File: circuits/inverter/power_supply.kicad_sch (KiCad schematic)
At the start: 44 parts

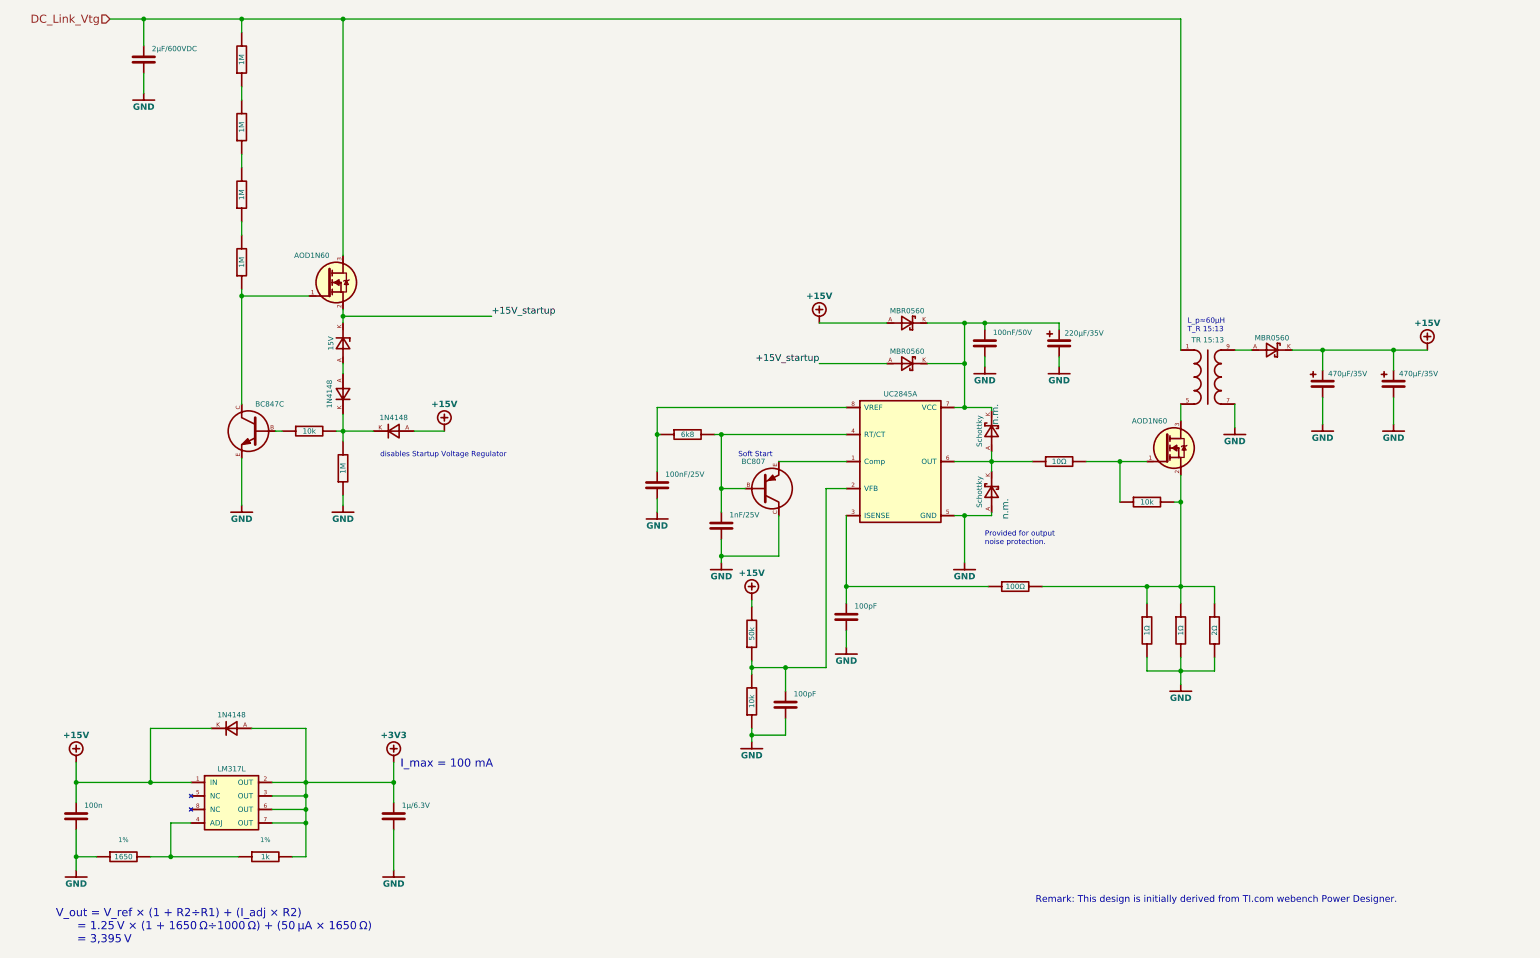
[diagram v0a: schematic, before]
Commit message: converts libraries to Kicad 6 format, updates bridge driver
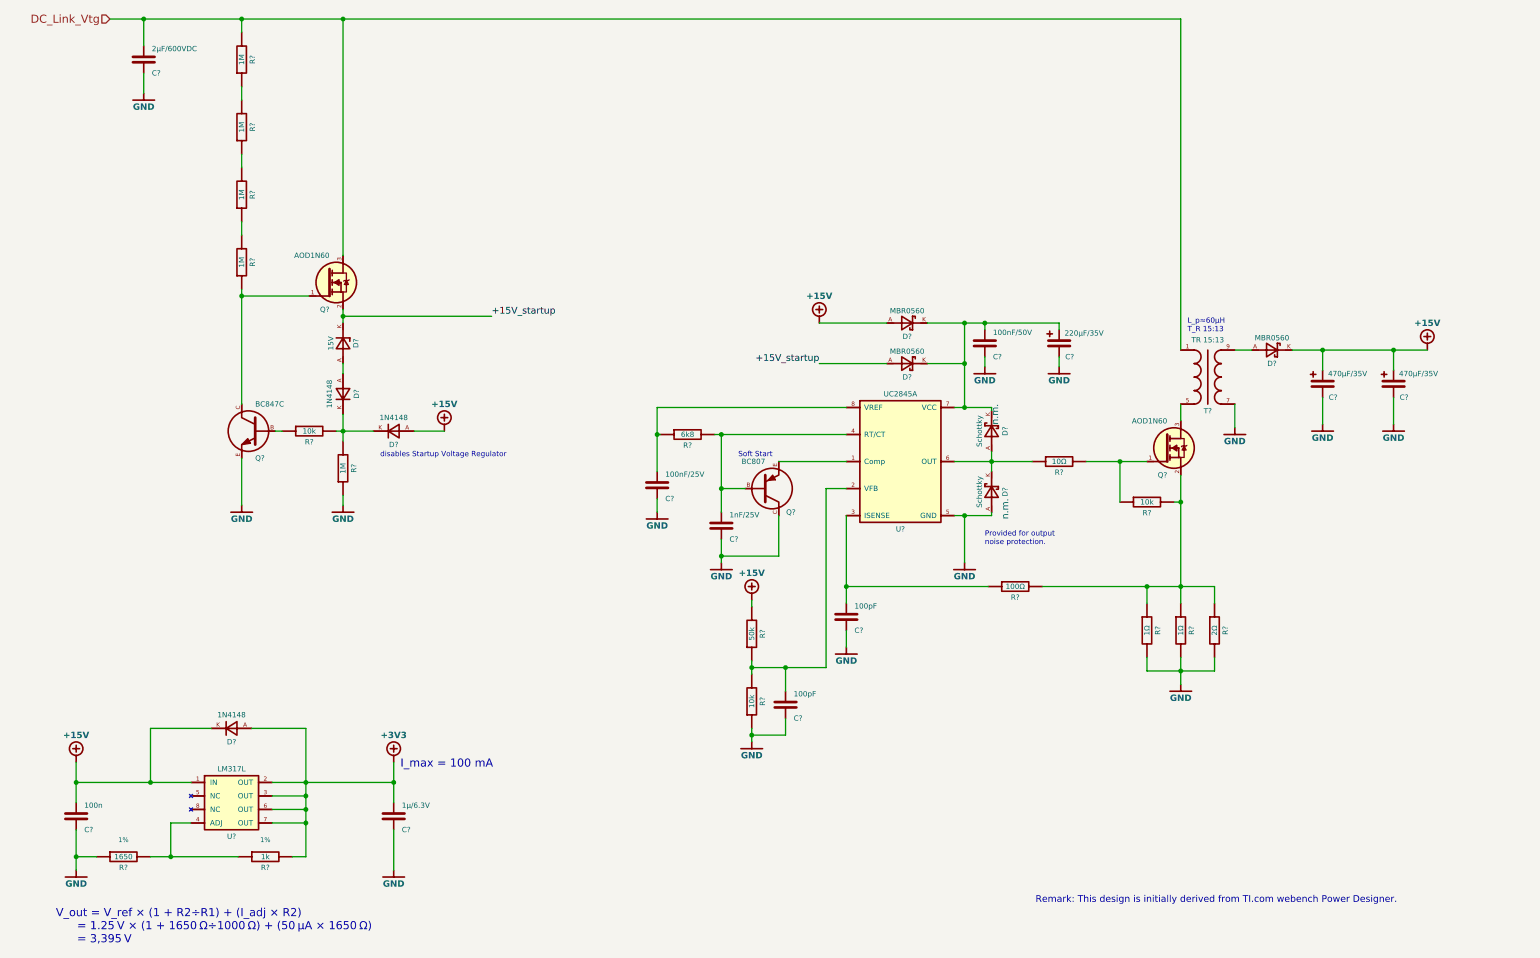
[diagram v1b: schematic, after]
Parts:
- gave numbers to parts that had none: 6

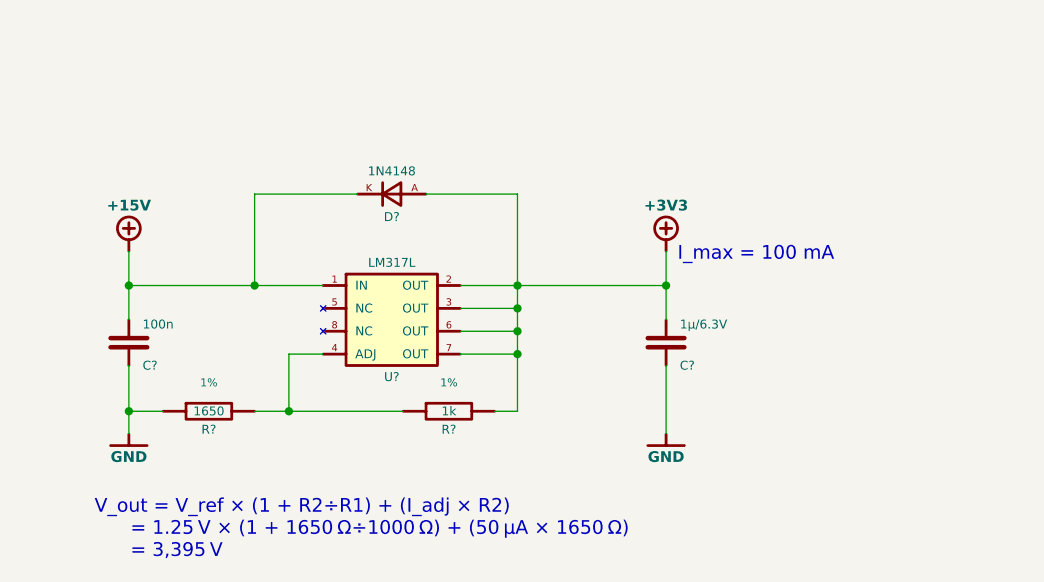
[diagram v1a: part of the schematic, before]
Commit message: updates circuits, adds linear regulator NCP1117
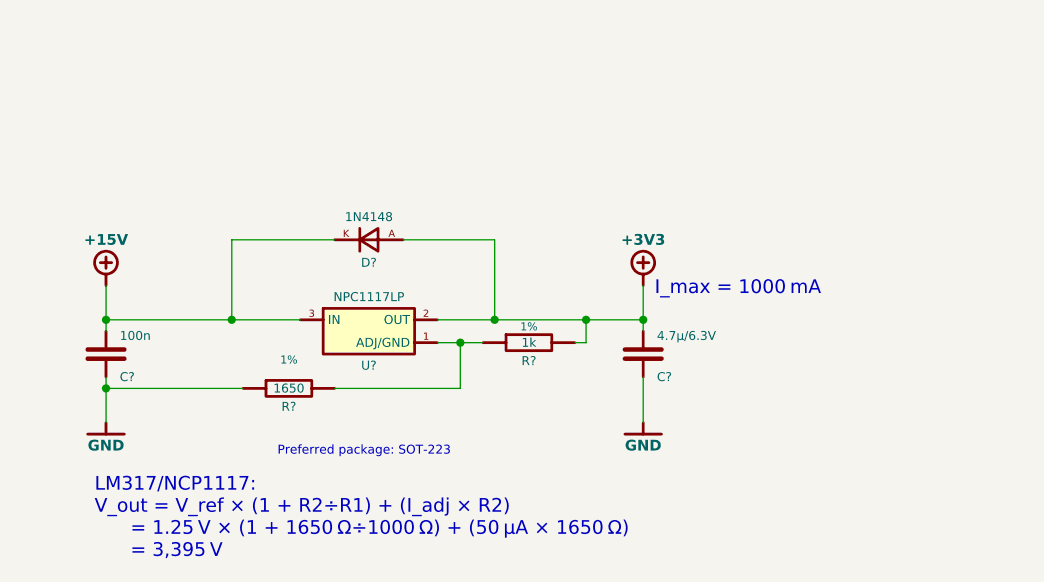
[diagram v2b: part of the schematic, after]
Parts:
- removed U?: LM317L, OSSI_standard_footprints:SOIC8, symbol lm317:LM317L
- added U?: NPC1117LP, symbol NCP1117LP:NPC1117LP
- C?: value 1µ/6.3V -> 4.7µ/6.3V
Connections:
- net +15V: now also U?.3 (IN)
- net +3V3: now also U?.2 (OUT)
- net at R?.1, R?.2: now also U?.1 (ADJ/GND)
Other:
- note added: "I_max = 1000 mA"
- note added: "LM317/NCP1117: V_out = V_ref × (1 + R2÷R1) + (I_adj × R2) = 1.25 V × (1 + 1650 Ω÷1000 Ω) + (50 µA × 1650 Ω) = 3,395 V"
- note added: "Preferred package: SOT-223"
- note removed: "I_max = 100 mA"
- note removed: "V_out = V_ref × (1 + R2÷R1) + (I_adj × R2) = 1.25 V × (1 + 1650 Ω÷1000 Ω) + (50 µA × 1650 Ω) = 3,395 V"
- moved on the sheet: C?, D?, R?

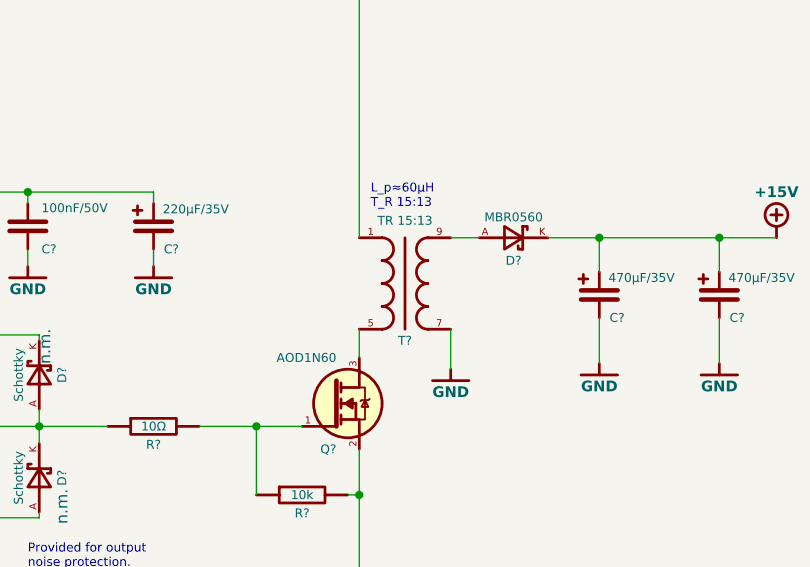
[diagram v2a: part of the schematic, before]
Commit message: converts the project to Kicad 7
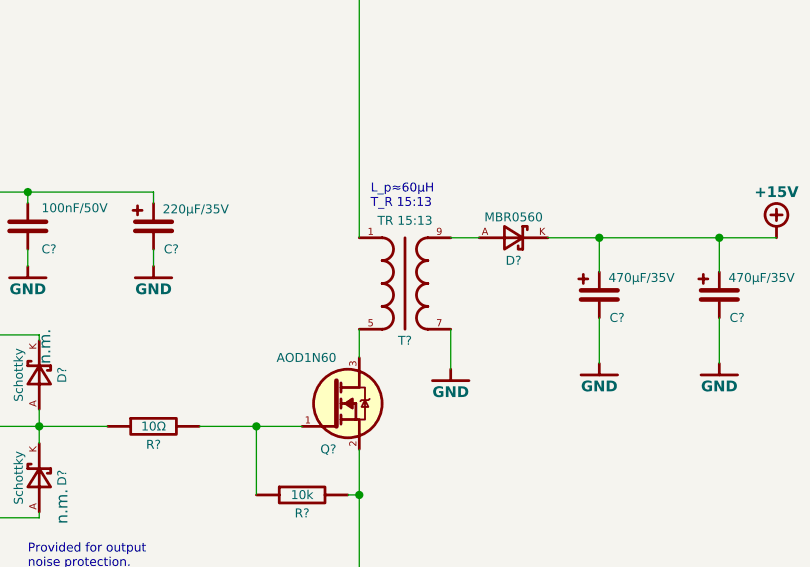
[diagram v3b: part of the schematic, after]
